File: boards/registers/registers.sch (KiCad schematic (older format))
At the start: 51 parts

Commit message: PCB started
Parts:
- added H1, H2, H3, H4: MountingHole_Pad, MountingHole:MountingHole_3.2mm_M3_DIN965_Pad, symbol Mechanical:MountingHole_Pad
- C1, C2, C3, C4: renamed from C?; footprint (none) -> Capacitor_SMD:C_0805_2012Metric
- D1, D10, D11, D12, D2, D3, D4, D5, D6, D7, D8, D9: renamed from D?; footprint (none) -> LED_SMD:LED_0805_2012Metric
- R1, R10, R11, R12, R13, R14, R15, R16, R17, R18, R19, R2, R20, R21, R22, R23, R24, R25, R26, R27, R28, R3, R4, R5, R6, R7, R8, R9: renamed from R?; footprint (none) -> Resistor_SMD:R_0805_2012Metric
- U1: renamed from U?; value 74LS08 -> 74ACT08; footprint (none) -> Package_SO:TSSOP-14_4.4x5mm_P0.65mm
- U2: renamed from U?; footprint (none) -> Package_SO:SO-20_12.8x7.5mm_P1.27mm
- U3: renamed from U?; footprint (none) -> Package_SO:SOIC-20W_7.5x12.8mm_P1.27mm
- U4: renamed from U?; value 74LS161 -> 74ACT161; footprint (none) -> Package_SO:SOIC-16_3.9x9.9mm_P1.27mm
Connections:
- net labels added: a_w_clk, b_w_clk

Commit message: PCB attempt
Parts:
- removed H1, H2, H3, H4: MountingHole_Pad, MountingHole:MountingHole_3.2mm_M3_DIN965_Pad, symbol Mechanical:MountingHole_Pad
- added H1, H2, H3, H4: MountingHole, MountingHole:MountingHole_3.2mm_M3_DIN965, symbol Mechanical:MountingHole
- U3: footprint Package_SO:SOIC-20W_7.5x12.8mm_P1.27mm -> Package_SO:TSSOP-20_4.4x6.5mm_P0.65mm
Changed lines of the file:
@@
 F 0 "U3" H 3750 3600 50  0000 C CNN
 F 1 "74AC273" H 3800 3500 50  0000 C CNN
-F 2 "Package_SO:SOIC-20W_7.5x12.8mm_P1.27mm" H 3350 4150 50  0001 C CNN
+F 2 "Package_SO:TSSOP-20_4.4x6.5mm_P0.65mm" H 3350 4150 50  0001 C CNN
 F 3 "https://assets.nexperia.com/documents/data-sheet/74HC_HCT273.pdf" H 3350 4150 50  0001 C CNN
 	1    3350 4150
@@
 	3850 4350 4300 4350
 Text Label 4250 3650 2    50   ~ 0
+ir_out3
+Text Label 4250 3750 2    50   ~ 0
+ir_out2
+Text Label 4250 3850 2    50   ~ 0
+ir_out1
+Text Label 4250 3950 2    50   ~ 0
 ir_out0
-Text Label 4250 3750 2    50   ~ 0
-ir_out1
-Text Label 4250 3850 2    50   ~ 0
-ir_out2
-Text Label 4250 3950 2    50   ~ 0
-ir_out3
 Text Label 4250 4050 2    50   ~ 0
 ir_out4
@@
 d7
 Text Label 2500 3650 0    50   ~ 0
+d3
+Text Label 2500 3750 0    50   ~ 0
+d2
+Text Label 2500 3850 0    50   ~ 0
+d1
+Text Label 2500 3950 0    50   ~ 0
 d0
-Text Label 2500 3750 0    50   ~ 0
-d1
-Text Label 2500 3850 0    50   ~ 0
-d2
-Text Label 2500 3950 0    50   ~ 0
-d3
 Text Label 2500 4050 0    50   ~ 0
 d4
@@
 Text Label 10750 5050 0    50   ~ 0
 b_w_clk
-$Comp
-L Mechanical:MountingHole_Pad H2
-U 1 1 5F02246C
-P 950 950
-F 0 "H2" H 1050 953 50  0000 L CNN
-F 1 "MountingHole_Pad" H 1050 908 50  0001 L CNN
-F 2 "MountingHole:MountingHole_3.2mm_M3_DIN965_Pad" H 950 950 50  0001 C CNN
-F 3 "~" H 950 950 50  0001 C CNN
-	1    950  950
-	1    0    0    -1
-$EndComp
-$Comp
-L power:GND #PWR02
-U 1 1 5F023377
-P 950 1050
-F 0 "#PWR02" H 950 800 50  0001 C CNN
-F 1 "GND" H 955 877 50  0000 C CNN
-F 2 "" H 950 1050 50  0001 C CNN
-F 3 "" H 950 1050 50  0001 C CNN
-	1    950  1050
-	1    0    0    -1
-$EndComp
-$Comp
-L Mechanical:MountingHole_Pad H3
-U 1 1 5F0249F8
-P 15500 950
-F 0 "H3" H 15600 953 50  0000 L CNN
-F 1 "MountingHole_Pad" H 15600 908 50  0001 L CNN
-F 2 "MountingHole:MountingHole_3.2mm_M3_DIN965_Pad" H 15500 950 50  0001 C CNN
-F 3 "~" H 15500 950 50  0001 C CNN
-	1    15500 950
-	1    0    0    -1
-$EndComp
-$Comp
-L power:GND #PWR040
-U 1 1 5F0249FE
-P 15500 1050
-F 0 "#PWR040" H 15500 800 50  0001 C CNN
-F 1 "GND" H 15505 877 50  0000 C CNN
-F 2 "" H 15500 1050 50  0001 C CNN
-F 3 "" H 15500 1050 50  0001 C CNN
-	1    15500 1050
-	1    0    0    -1
-$EndComp
-$Comp
-L Mechanical:MountingHole_Pad H1
-U 1 1 5F02D6E1
-P 850 9100
-F 0 "H1" H 950 9103 50  0000 L CNN
-F 1 "MountingHole_Pad" H 950 9058 50  0001 L CNN
-F 2 "MountingHole:MountingHole_3.2mm_M3_DIN965_Pad" H 850 9100 50  0001 C CNN
-F 3 "~" H 850 9100 50  0001 C CNN
-	1    850  9100
-	1    0    0    -1
-$EndComp
-$Comp
-L power:GND #PWR01
-U 1 1 5F02D6E7
-P 850 9200
-F 0 "#PWR01" H 850 8950 50  0001 C CNN
-F 1 "GND" H 855 9027 50  0000 C CNN
-F 2 "" H 850 9200 50  0001 C CNN
-F 3 "" H 850 9200 50  0001 C CNN
-	1    850  9200
-	1    0    0    -1
-$EndComp
-$Comp
-L Mechanical:MountingHole_Pad H4
-U 1 1 5F035F46
-P 15500 9400
-F 0 "H4" H 15600 9403 50  0000 L CNN
-F 1 "MountingHole_Pad" H 15600 9358 50  0001 L CNN
-F 2 "MountingHole:MountingHole_3.2mm_M3_DIN965_Pad" H 15500 9400 50  0001 C CNN
-F 3 "~" H 15500 9400 50  0001 C CNN
-	1    15500 9400
-	1    0    0    -1
-$EndComp
-$Comp
-L power:GND #PWR041
-U 1 1 5F035F4C
-P 15500 9500
-F 0 "#PWR041" H 15500 9250 50  0001 C CNN
-F 1 "GND" H 15505 9327 50  0000 C CNN
-F 2 "" H 15500 9500 50  0001 C CNN
-F 3 "" H 15500 9500 50  0001 C CNN
-	1    15500 9500
-	1    0    0    -1
-$EndComp
 Wire Bus Line
 	2350 6050 2350 6700
@@
 Wire Bus Line
 	2400 1150 2400 4750
+$Comp
+L Mechanical:MountingHole H1
+U 1 1 5F1D6D3E
+P 700 750
+F 0 "H1" H 800 796 50  0000 L CNN
+F 1 "MountingHole" H 800 705 50  0000 L CNN
+F 2 "MountingHole:MountingHole_3.2mm_M3_DIN965" H 700 750 50  0001 C CNN
+F 3 "~" H 700 750 50  0001 C CNN
+	1    700  750
+	1    0    0    -1
+$EndComp
+$Comp
+L Mechanical:MountingHole H4
+U 1 1 5F1D725A
+P 15400 700
+F 0 "H4" H 15500 746 50  0000 L CNN
+F 1 "MountingHole" H 15500 655 50  0000 L CNN
+F 2 "MountingHole:MountingHole_3.2mm_M3_DIN965" H 15400 700 50  0001 C CNN
+F 3 "~" H 15400 700 50  0001 C CNN
+	1    15400 700
+	1    0    0    -1
+$EndComp
+$Comp
+L Mechanical:MountingHole H2
+U 1 1 5F1D7797
+P 850 9400
+F 0 "H2" H 950 9446 50  0000 L CNN
+F 1 "MountingHole" H 950 9355 50  0000 L CNN
+F 2 "MountingHole:MountingHole_3.2mm_M3_DIN965" H 850 9400 50  0001 C CNN
+F 3 "~" H 850 9400 50  0001 C CNN
+	1    850  9400
+	1    0    0    -1
+$EndComp
+$Comp
+L Mechanical:MountingHole H3
+U 1 1 5F1D7D9A
+P 15350 9500
+F 0 "H3" H 15450 9546 50  0000 L CNN
+F 1 "MountingHole" H 15450 9455 50  0000 L CNN
+F 2 "MountingHole:MountingHole_3.2mm_M3_DIN965" H 15350 9500 50  0001 C CNN
+F 3 "~" H 15350 9500 50  0001 C CNN
+	1    15350 9500
+	1    0    0    -1
+$EndComp
 $EndSCHEMATC

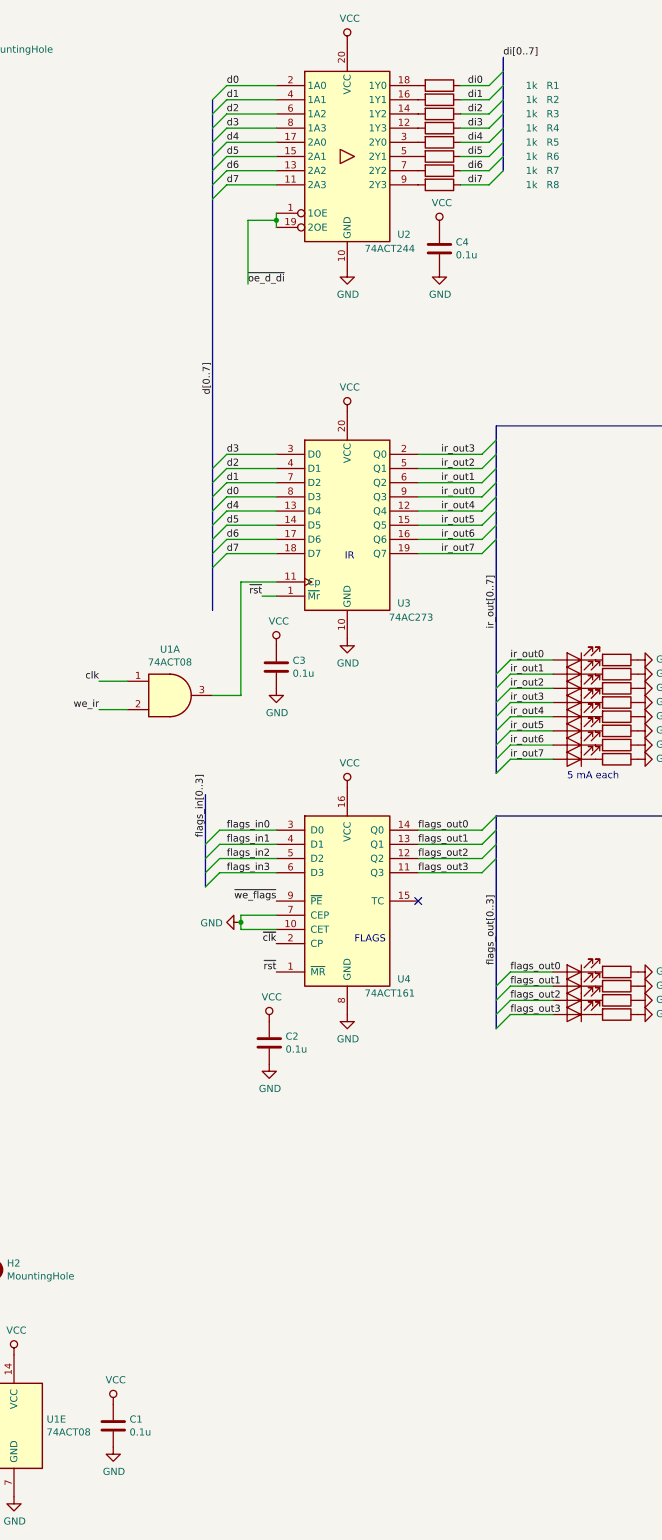
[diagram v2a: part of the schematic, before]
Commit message: CPU registers board
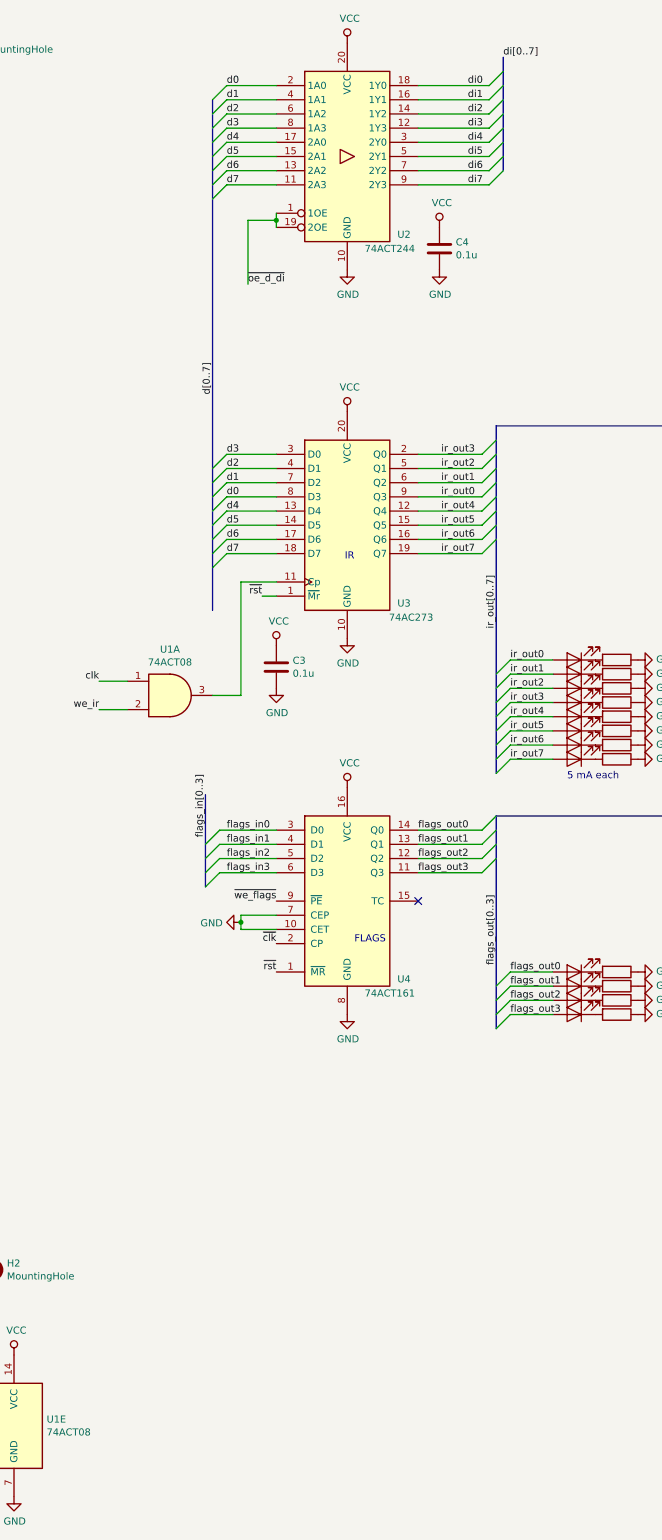
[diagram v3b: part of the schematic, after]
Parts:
- removed C1, C2: 0.1u, Capacitor_SMD:C_0805_2012Metric, symbol Device:C
- removed R1, R2, R3, R4, R5, R6, R7, R8: 1k, Resistor_SMD:R_0805_2012Metric, symbol Device:R
- U2: footprint Package_SO:SO-20_12.8x7.5mm_P1.27mm -> Package_SO:TSSOP-20_4.4x6.5mm_P0.65mm
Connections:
- net di0: now also U2.18 (1Y0)
- net di1: now also U2.16 (1Y1)
- net di2: now also U2.14 (1Y2)
- net di3: now also U2.12 (1Y3)
- net di4: now also U2.3 (2Y0)
- net di5: now also U2.5 (2Y1)
- net di6: now also U2.7 (2Y2)
- net di7: now also U2.9 (2Y3)
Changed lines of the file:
@@
 F 0 "U2" H 3750 1000 50  0000 C CNN
 F 1 "74ACT244" H 3650 900 50  0000 C CNN
-F 2 "Package_SO:SO-20_12.8x7.5mm_P1.27mm" H 3350 1550 50  0001 C CNN
+F 2 "Package_SO:TSSOP-20_4.4x6.5mm_P0.65mm" H 3350 1550 50  0001 C CNN
 F 3 "https://assets.nexperia.com/documents/data-sheet/74HC_HCT244.pdf" H 3350 1550 50  0001 C CNN
 	1    3350 1550
@@
 Entry Wire Line
 	4350 1750 4450 1650
-Wire Wire Line
-	4350 1750 4150 1750
-Wire Wire Line
-	4150 1650 4350 1650
-Wire Wire Line
-	4350 1550 4150 1550
-Wire Wire Line
-	4150 1450 4350 1450
-Wire Wire Line
-	4350 1350 4150 1350
-Wire Wire Line
-	4150 1250 4350 1250
-Wire Wire Line
-	4350 1150 4150 1150
-Wire Wire Line
-	4150 1050 4350 1050
 Text Label 4450 850  0    50   ~ 0
 di[0..7]
@@
 ~we_flags
 $Comp
-L 74xx:74LS161 U4
-U 1 1 5E857F06
-P 3350 6800
-F 0 "U4" H 3750 6250 50  0000 C CNN
-F 1 "74ACT161" H 3650 6150 50  0000 C CNN
-F 2 "Package_SO:SOIC-16_3.9x9.9mm_P1.27mm" H 3350 6800 50  0001 C CNN
-F 3 "http://www.ti.com/lit/gpn/sn74LS161" H 3350 6800 50  0001 C CNN
-	1    3350 6800
-	1    0    0    -1
-$EndComp
-$Comp
 L power:GND #PWR07
 U 1 1 5E85E09A
@@
 $EndComp
 $Comp
-L Device:C C1
-U 1 1 5E90E340
-P 1700 10500
-F 0 "C1" H 1815 10546 50  0000 L CNN
-F 1 "0.1u" H 1815 10455 50  0000 L CNN
-F 2 "Capacitor_SMD:C_0805_2012Metric" H 1738 10350 50  0001 C CNN
-F 3 "~" H 1700 10500 50  0001 C CNN
-	1    1700 10500
-	1    0    0    -1
-$EndComp
-$Comp
-L power:VCC #PWR05
-U 1 1 5E90E95C
-P 1700 10350
-F 0 "#PWR05" H 1700 10200 50  0001 C CNN
-F 1 "VCC" H 1717 10523 50  0000 C CNN
-F 2 "" H 1700 10350 50  0001 C CNN
-F 3 "" H 1700 10350 50  0001 C CNN
-	1    1700 10350
-	1    0    0    -1
-$EndComp
-$Comp
-L power:GND #PWR06
-U 1 1 5E90EDAB
-P 1700 10650
-F 0 "#PWR06" H 1700 10400 50  0001 C CNN
-F 1 "GND" H 1705 10477 50  0000 C CNN
-F 2 "" H 1700 10650 50  0001 C CNN
-F 3 "" H 1700 10650 50  0001 C CNN
-	1    1700 10650
-	1    0    0    -1
-$EndComp
-$Comp
-L Device:C C2
-U 1 1 5E91148F
-P 2800 7800
-F 0 "C2" H 2915 7846 50  0000 L CNN
-F 1 "0.1u" H 2915 7755 50  0000 L CNN
-F 2 "Capacitor_SMD:C_0805_2012Metric" H 2838 7650 50  0001 C CNN
-F 3 "~" H 2800 7800 50  0001 C CNN
-	1    2800 7800
-	1    0    0    -1
-$EndComp
-$Comp
-L power:VCC #PWR08
-U 1 1 5E911495
-P 2800 7650
-F 0 "#PWR08" H 2800 7500 50  0001 C CNN
-F 1 "VCC" H 2817 7823 50  0000 C CNN
-F 2 "" H 2800 7650 50  0001 C CNN
-F 3 "" H 2800 7650 50  0001 C CNN
-	1    2800 7650
-	1    0    0    -1
-$EndComp
-$Comp
-L power:GND #PWR09
-U 1 1 5E91149B
-P 2800 7950
-F 0 "#PWR09" H 2800 7700 50  0001 C CNN
-F 1 "GND" H 2805 7777 50  0000 C CNN
-F 2 "" H 2800 7950 50  0001 C CNN
-F 3 "" H 2800 7950 50  0001 C CNN
-	1    2800 7950
-	1    0    0    -1
-$EndComp
-$Comp
 L Device:C C3
 U 1 1 5E917009
@@
 	1    4000 2350
 	1    0    0    -1
-$EndComp
-$Comp
-L Device:R R?
-U 1 1 5E9A723F
-P 4000 1050
-AR Path="/5E7CA397/5E9A723F" Ref="R?"  Part="1"
-AR Path="/5E9A723F" Ref="R1"  Part="1"
-F 0 "R1" V 4000 1850 50  0000 C CNN
-F 1 "1k" V 4000 1700 50  0000 C CNN
-F 2 "Resistor_SMD:R_0805_2012Metric" V 3930 1050 50  0001 C CNN
-F 3 "~" H 4000 1050 50  0001 C CNN
-	1    4000 1050
-	0    1    1    0
-$EndComp
-$Comp
-L Device:R R?
-U 1 1 5E9A7245
-P 4000 1150
-AR Path="/5E7CA397/5E9A7245" Ref="R?"  Part="1"
-AR Path="/5E9A7245" Ref="R2"  Part="1"
-F 0 "R2" V 4000 1950 50  0000 C CNN
-F 1 "1k" V 4000 1800 50  0000 C CNN
-F 2 "Resistor_SMD:R_0805_2012Metric" V 3930 1150 50  0001 C CNN
-F 3 "~" H 4000 1150 50  0001 C CNN
-	1    4000 1150
-	0    1    1    0
-$EndComp
-$Comp
-L Device:R R?
-U 1 1 5E9A724B
-P 4000 1250
-AR Path="/5E7CA397/5E9A724B" Ref="R?"  Part="1"
-AR Path="/5E9A724B" Ref="R3"  Part="1"
-F 0 "R3" V 4000 2050 50  0000 C CNN
-F 1 "1k" V 4000 1900 50  0000 C CNN
-F 2 "Resistor_SMD:R_0805_2012Metric" V 3930 1250 50  0001 C CNN
-F 3 "~" H 4000 1250 50  0001 C CNN
-	1    4000 1250
-	0    1    1    0
-$EndComp
-$Comp
-L Device:R R?
-U 1 1 5E9A7251
-P 4000 1350
-AR Path="/5E7CA397/5E9A7251" Ref="R?"  Part="1"
-AR Path="/5E9A7251" Ref="R4"  Part="1"
-F 0 "R4" V 4000 2150 50  0000 C CNN
-F 1 "1k" V 4000 2000 50  0000 C CNN
-F 2 "Resistor_SMD:R_0805_2012Metric" V 3930 1350 50  0001 C CNN
-F 3 "~" H 4000 1350 50  0001 C CNN
-	1    4000 1350
-	0    1    1    0
-$EndComp
-$Comp
-L Device:R R?
-U 1 1 5E9A7257
-P 4000 1450
-AR Path="/5E7CA397/5E9A7257" Ref="R?"  Part="1"
-AR Path="/5E9A7257" Ref="R5"  Part="1"
-F 0 "R5" V 4000 2250 50  0000 C CNN
-F 1 "1k" V 4000 2100 50  0000 C CNN
-F 2 "Resistor_SMD:R_0805_2012Metric" V 3930 1450 50  0001 C CNN
-F 3 "~" H 4000 1450 50  0001 C CNN
-	1    4000 1450
-	0    1    1    0
-$EndComp
-$Comp
-L Device:R R?
-U 1 1 5E9A725D
-P 4000 1550
-AR Path="/5E7CA397/5E9A725D" Ref="R?"  Part="1"
-AR Path="/5E9A725D" Ref="R6"  Part="1"
-F 0 "R6" V 4000 2350 50  0000 C CNN
-F 1 "1k" V 4000 2200 50  0000 C CNN
-F 2 "Resistor_SMD:R_0805_2012Metric" V 3930 1550 50  0001 C CNN
-F 3 "~" H 4000 1550 50  0001 C CNN
-	1    4000 1550
-	0    1    1    0
-$EndComp
-$Comp
-L Device:R R?
-U 1 1 5E9A7263
-P 4000 1650
-AR Path="/5E7CA397/5E9A7263" Ref="R?"  Part="1"
-AR Path="/5E9A7263" Ref="R7"  Part="1"
-F 0 "R7" V 4000 2450 50  0000 C CNN
-F 1 "1k" V 4000 2300 50  0000 C CNN
-F 2 "Resistor_SMD:R_0805_2012Metric" V 3930 1650 50  0001 C CNN
-F 3 "~" H 4000 1650 50  0001 C CNN
-	1    4000 1650
-	0    1    1    0
-$EndComp
-$Comp
-L Device:R R?
-U 1 1 5E9A7269
-P 4000 1750
-AR Path="/5E7CA397/5E9A7269" Ref="R?"  Part="1"
-AR Path="/5E9A7269" Ref="R8"  Part="1"
-F 0 "R8" V 4000 2550 50  0000 C CNN
-F 1 "1k" V 4000 2400 50  0000 C CNN
-F 2 "Resistor_SMD:R_0805_2012Metric" V 3930 1750 50  0001 C CNN
-F 3 "~" H 4000 1750 50  0001 C CNN
-	1    4000 1750
-	0    1    1    0
 $EndComp
 $Sheet
@@
 Text Label 10750 5050 0    50   ~ 0
 b_w_clk
-Wire Bus Line
-	2350 6050 2350 6700
-Wire Bus Line
-	13750 4550 13750 5950
-Wire Bus Line
-	4400 6200 4400 7700
-Wire Bus Line
-	4450 850  4450 1650
-Wire Bus Line
-	13200 5950 13200 7650
-Wire Bus Line
-	4400 3450 4400 5900
-Wire Bus Line
-	2400 1150 2400 4750
 $Comp
 L Mechanical:MountingHole H1
@@
 	1    0    0    -1
 $EndComp
+Wire Wire Line
+	3850 1050 4350 1050
+Wire Wire Line
+	3850 1150 4350 1150
+Wire Wire Line
+	3850 1250 4350 1250
+Wire Wire Line
+	3850 1350 4350 1350
+Wire Wire Line
+	3850 1450 4350 1450
+Wire Wire Line
+	3850 1550 4350 1550
+Wire Wire Line
+	3850 1650 4350 1650
+Wire Wire Line
+	3850 1750 4350 1750
+$Comp
+L 74xx:74LS161 U4
+U 1 1 5E857F06
+P 3350 6800
+F 0 "U4" H 3750 6250 50  0000 C CNN
+F 1 "74ACT161" H 3650 6150 50  0000 C CNN
+F 2 "Package_SO:SOIC-16_3.9x9.9mm_P1.27mm" H 3350 6800 50  0001 C CNN
+F 3 "http://www.ti.com/lit/gpn/sn74LS161" H 3350 6800 50  0001 C CNN
+	1    3350 6800
+	1    0    0    -1
+$EndComp
+Wire Bus Line
+	13750 4550 13750 5950
+Wire Bus Line
+	2350 6050 2350 6700
+Wire Bus Line
+	4400 6200 4400 7700
+Wire Bus Line
+	13200 5950 13200 7650
+Wire Bus Line
+	4450 850  4450 1650
+Wire Bus Line
+	2400 1150 2400 4750
+Wire Bus Line
+	4400 3450 4400 5900
 $EndSCHEMATC

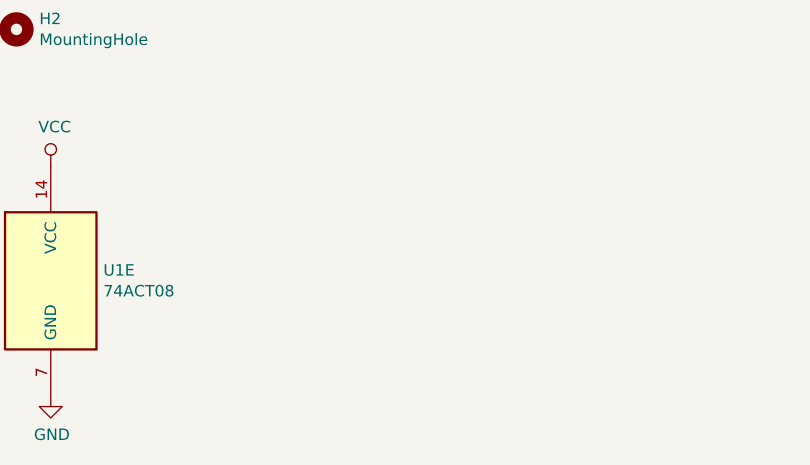
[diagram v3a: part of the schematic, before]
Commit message: Remove RAM and ROM from the registers board, board rework in progress
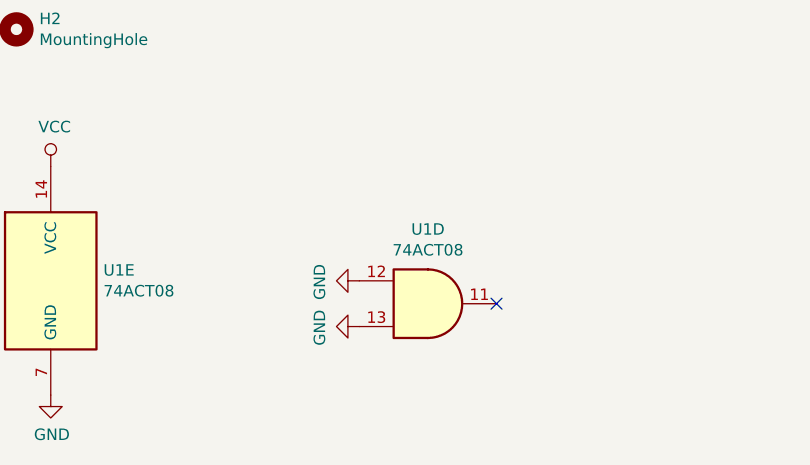
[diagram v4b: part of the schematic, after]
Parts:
- added unit 4 of U1
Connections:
- net GND: now also U1.12, U1.13
- no-connect marks 1 -> 2
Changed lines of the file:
@@
 	1    0    0    -1
 $EndComp
+$Comp
+L 74xx:74LS08 U1
+U 4 1 605886B2
+P 2650 10600
+F 0 "U1" H 2650 10925 50  0000 C CNN
+F 1 "74ACT08" H 2650 10834 50  0000 C CNN
+F 2 "Package_SO:TSSOP-14_4.4x5mm_P0.65mm" H 2650 10600 50  0001 C CNN
+F 3 "http://www.ti.com/lit/gpn/sn74LS08" H 2650 10600 50  0001 C CNN
+	4    2650 10600
+	1    0    0    -1
+$EndComp
+$Comp
+L power:GND #PWR08
+U 1 1 6058DCB0
+P 2350 10500
+F 0 "#PWR08" H 2350 10250 50  0001 C CNN
+F 1 "GND" H 2355 10327 50  0000 C CNN
+F 2 "" H 2350 10500 50  0001 C CNN
+F 3 "" H 2350 10500 50  0001 C CNN
+	1    2350 10500
+	0    1    1    0
+$EndComp
+$Comp
+L power:GND #PWR09
+U 1 1 6058E349
+P 2350 10700
+F 0 "#PWR09" H 2350 10450 50  0001 C CNN
+F 1 "GND" H 2355 10527 50  0000 C CNN
+F 2 "" H 2350 10700 50  0001 C CNN
+F 3 "" H 2350 10700 50  0001 C CNN
+	1    2350 10700
+	0    1    1    0
+$EndComp
+NoConn ~ 2950 10600
 Wire Bus Line
 	13750 4550 13750 5950
